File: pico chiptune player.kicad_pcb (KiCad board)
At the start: 4 copper layers, 118 x 92 mm, 52 parts, among them J2 MicroSD, J3 Speaker_L, J4 Speaker_R, SW1 Play / Pause, SW2 Next, SW3 Previous, U1 YM2149F, U2 0.96"OLED_I2C, U3 PAM8403, U4 YM2149F

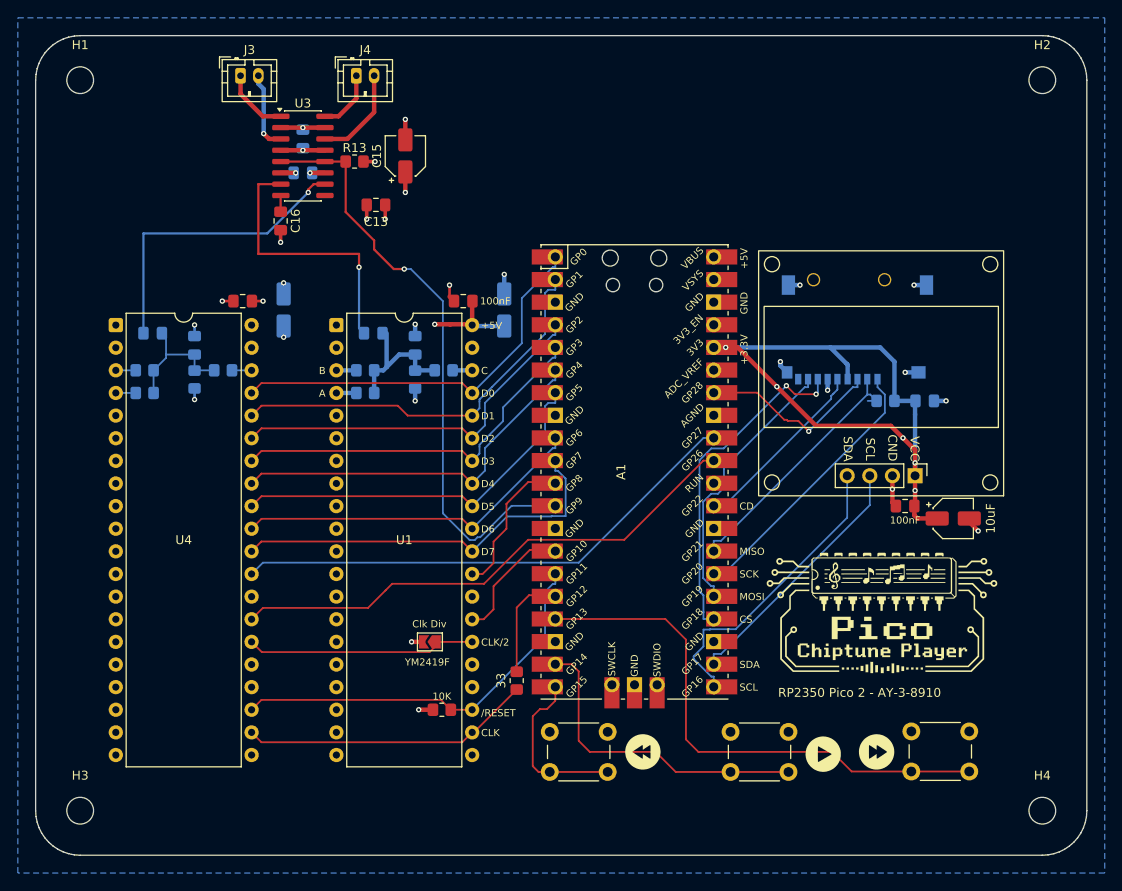
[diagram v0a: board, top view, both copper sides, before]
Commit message: feat(hw): upgrade to Rev 0.7 with bare RP2354A, USB-C 3-stage sequencer, and 4-mode 74HCT4053D stereo/mono mixing matrix
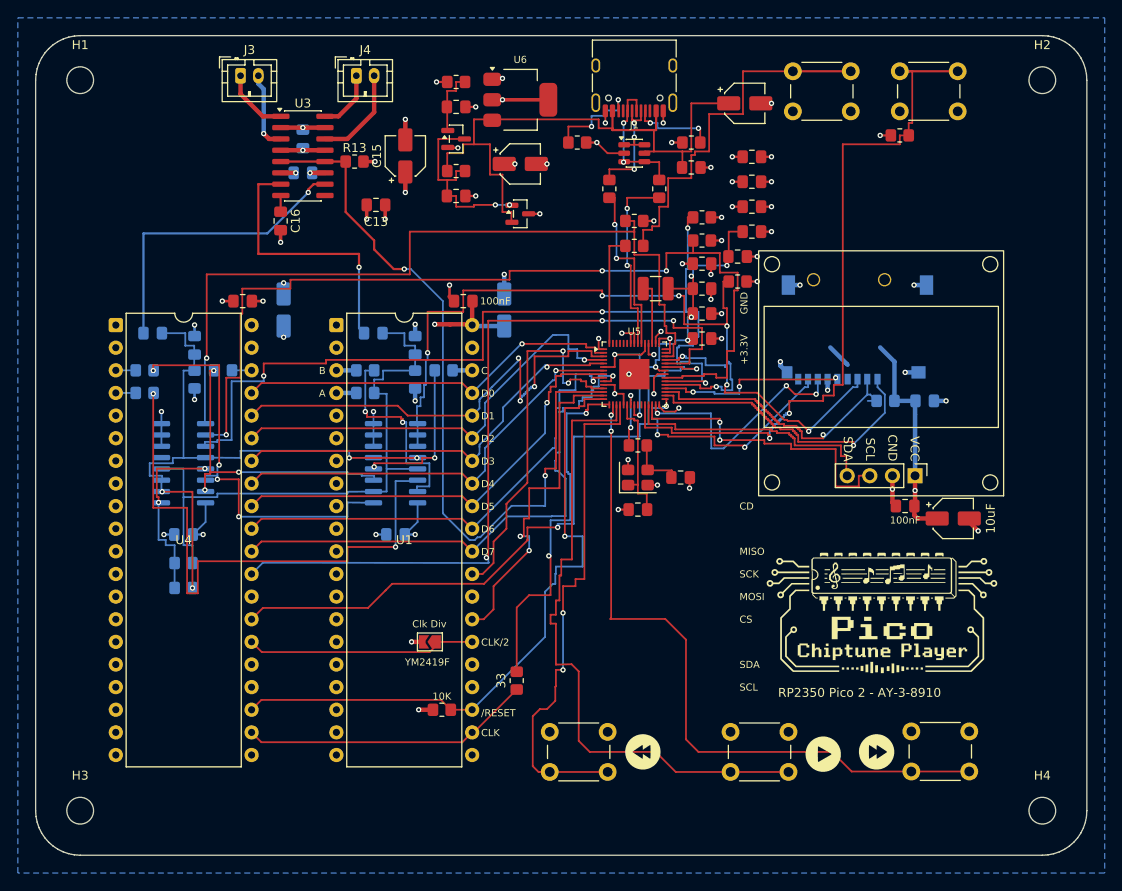
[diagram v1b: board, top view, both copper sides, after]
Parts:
- removed A1: RaspberryPi_Pico 2, TMCu Module:RPi_Pico_SMD_TH
- added C17: 10uF, CP_Elec_4x5.4, F.Cu at (157.6, 57.6)
- added C18: 100nF, C_0805_2012Metric_Pad1.18x1.45mm_HandSolder, F.Cu at (151.6, 64.8)
- added C19: 10uF, CP_Elec_4x5.4, F.Cu at (132.4, 64.4)
- added C20: 15pF, C_0805_2012Metric_Pad1.18x1.45mm_HandSolder, F.Cu at (145.6, 103.2)
- added C21: 15pF, C_0805_2012Metric_Pad1.18x1.45mm_HandSolder, F.Cu at (150.4, 99.6)
- added C22: 1uF, C_0805_2012Metric_Pad1.18x1.45mm_HandSolder, F.Cu at (152.8, 75.6)
- added C23: 4.7uF, C_0805_2012Metric_Pad1.18x1.45mm_HandSolder, F.Cu at (152.8, 78.4)
- added C24: 4.7uF, C_0805_2012Metric_Pad1.18x1.45mm_HandSolder, F.Cu at (152.8, 81.2)
- added C25: 100nF, C_0805_2012Metric_Pad1.18x1.45mm_HandSolder, F.Cu at (152.8, 84.0)
- added C26: 100nF, C_0805_2012Metric_Pad1.18x1.45mm_HandSolder, F.Cu at (158.4, 72.0)
- added C27: 100nF, C_0805_2012Metric_Pad1.18x1.45mm_HandSolder, F.Cu at (156.8, 74.8)
- added C28: 100nF, C_0805_2012Metric_Pad1.18x1.45mm_HandSolder, F.Cu at (158.4, 63.6)
- added C29: 100nF, C_0805_2012Metric_Pad1.18x1.45mm_HandSolder, F.Cu at (158.4, 66.4)
- added C30: 100nF, C_0805_2012Metric_Pad1.18x1.45mm_HandSolder, F.Cu at (158.4, 69.2)
- added C31: 100nF, C_0805_2012Metric_Pad1.18x1.45mm_HandSolder, F.Cu at (125.2, 58.0)
- added C32: 10nF, C_0805_2012Metric_Pad1.18x1.45mm_HandSolder, F.Cu at (125.2, 68.0)
- added C33: 100nF, C_0805_2012Metric_Pad1.18x1.45mm_HandSolder, B.Cu at (94.6, 106.0)
- added C34: 100nF, C_0805_2012Metric_Pad1.18x1.45mm_HandSolder, B.Cu at (118.4, 106.0)
- added D1: USBLC6-2SC6, SOT-23-6, F.Cu at (145.2, 63.2)
- added J1: USB_C_5V3A, USB_C_Receptacle_HRO_TYPE-C-31-M-12, F.Cu at (145.2, 54.4)
- added L1: 3.3uH, L_1210_3225Metric, F.Cu at (147.6, 78.4)
- added Q1: AO3401A, SOT-23, F.Cu at (132.4, 70.0)
- added Q2: 2N7002, SOT-23, F.Cu at (125.2, 61.6)
- added R14: 1k, R_0805_2012Metric_Pad1.20x1.40mm_HandSolder, B.Cu at (94.6, 109.2)
- added R15: 1k, R_0805_2012Metric_Pad1.20x1.40mm_HandSolder, B.Cu at (94.6, 112.0)
- added R16: 1k, R_0805_2012Metric_Pad1.20x1.40mm_HandSolder, F.Cu at (145.6, 96.0)
- added R17: 27, R_0805_2012Metric_Pad1.20x1.40mm_HandSolder, F.Cu at (142.4, 67.2)
- added R18: 27, R_0805_2012Metric_Pad1.20x1.40mm_HandSolder, F.Cu at (148.0, 67.2)
- added R19: 10K, R_0805_2012Metric_Pad1.20x1.40mm_HandSolder, F.Cu at (175.0, 61.2)
- added R20: 1k, R_0805_2012Metric_Pad1.20x1.40mm_HandSolder, F.Cu at (145.2, 73.6)
- added R21: 5.1k, R_0805_2012Metric_Pad1.20x1.40mm_HandSolder, F.Cu at (151.6, 62.0)
- added R22: 5.1k, R_0805_2012Metric_Pad1.20x1.40mm_HandSolder, F.Cu at (138.8, 62.0)
- added R23: 47K, R_0805_2012Metric_Pad1.20x1.40mm_HandSolder, F.Cu at (125.2, 55.2)
- added R24: 10K, R_0805_2012Metric_Pad1.20x1.40mm_HandSolder, F.Cu at (156.8, 77.6)
- added R25: 10K, R_0805_2012Metric_Pad1.20x1.40mm_HandSolder, F.Cu at (152.8, 70.4)
- added R26: 10K, R_0805_2012Metric_Pad1.20x1.40mm_HandSolder, F.Cu at (152.8, 73.0)
- added R27: 10K, R_0805_2012Metric_Pad1.20x1.40mm_HandSolder, F.Cu at (145.2, 70.8)
- added R28: 100K, R_0805_2012Metric_Pad1.20x1.40mm_HandSolder, F.Cu at (125.2, 65.2)
- added SW4: BOOTSEL, SW_PUSH_6mm, F.Cu at (163.0, 54.0)
- added SW5: RESET, SW_PUSH_6mm, F.Cu at (175.0, 54.0)
- added U5: RP2354A, QFN-60-1EP_7x7mm_P0.4mm_EP3.4x3.4mm, F.Cu at (145.2, 88.0)
- added U6: AMS1117-3.3, SOT-223-3_TabPin2, F.Cu at (132.4, 57.2)
- added U8: 74HCT4053D, SOIC-16_3.9x9.9mm_P1.27mm, B.Cu at (94.6, 98.0)
- added U9: 74HCT4053D, SOIC-16_3.9x9.9mm_P1.27mm, B.Cu at (118.4, 98.0)
- added Y1: 12MHz, Crystal_SMD_3225-4Pin_3.2x2.5mm, F.Cu at (145.6, 99.6)
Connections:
- C3 pad 1: Net-(C3-Pad1) -> /MIX1
- C4 pad 1: Net-(C3-Pad1) -> /MIX1
- J2 pad 9: (no net) -> unconnected-(J2-Card_Detect-Pad9)
- R10 pad 2: /MIX2 -> /NODE_B_PAN
- R11 pad 2: /MIX2 -> /NODE_C_PAN
- R2 pad 2: Net-(A1-GPIO12) -> /MCU_CLK
- R4 pad 2: Net-(C3-Pad1) -> /MIX1
- R5 pad 2: Net-(C3-Pad1) -> /B1_SUM
- R7 pad 2: Net-(C3-Pad1) -> /C1_SUM
- R8 pad 1: Net-(C3-Pad1) -> /MIX1
- R9 pad 2: /MIX2 -> /A2_SUM
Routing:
- net /MUX_C_CEN: track 0.00 -> 104.5 mm, vias 0 -> 3
- net /MUX_B_CEN: track 0.00 -> 100.7 mm, vias 0 -> 4
- net /MUX_MONO: track 0.00 -> 91.9 mm, vias 0 -> 1
- net /MCU_RUN: track 0.00 -> 81.9 mm, vias 0 -> 2
- net /MUX_PAN: track 0.00 -> 78.8 mm, vias 0 -> 5
- net /MIX1: track 0.00 -> 70.2 mm
- net VBUS: track 0.00 -> 67.6 mm
- net /A2_SUM: track 0.00 -> 64.8 mm, vias 0 -> 2
- net /MIX2: track 14.5 -> 70.3 mm, vias 0 -> 4
- net +1V1: track 0.00 -> 50.6 mm, vias 0 -> 7
- net GND: track 42.9 -> 90.2 mm, vias 24 -> 57
- net /NODE_B_PAN: track 0.00 -> 46.4 mm, vias 0 -> 4
- net /BOOT_BTN: track 0.00 -> 42.9 mm
- net /MCU_CLK: track 0.00 -> 40.8 mm, vias 0 -> 2
- net /SW_PREV: track 19.1 -> 58.0 mm, vias 0 -> 2
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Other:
- board text removed: "+5V"
- board text removed: "YM2149F"
